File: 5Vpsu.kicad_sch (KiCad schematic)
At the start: 20 parts, among them J8 Conn_01x04_Pin, J9 Conn_01x04_Pin, U7 TPS54360BDDAR

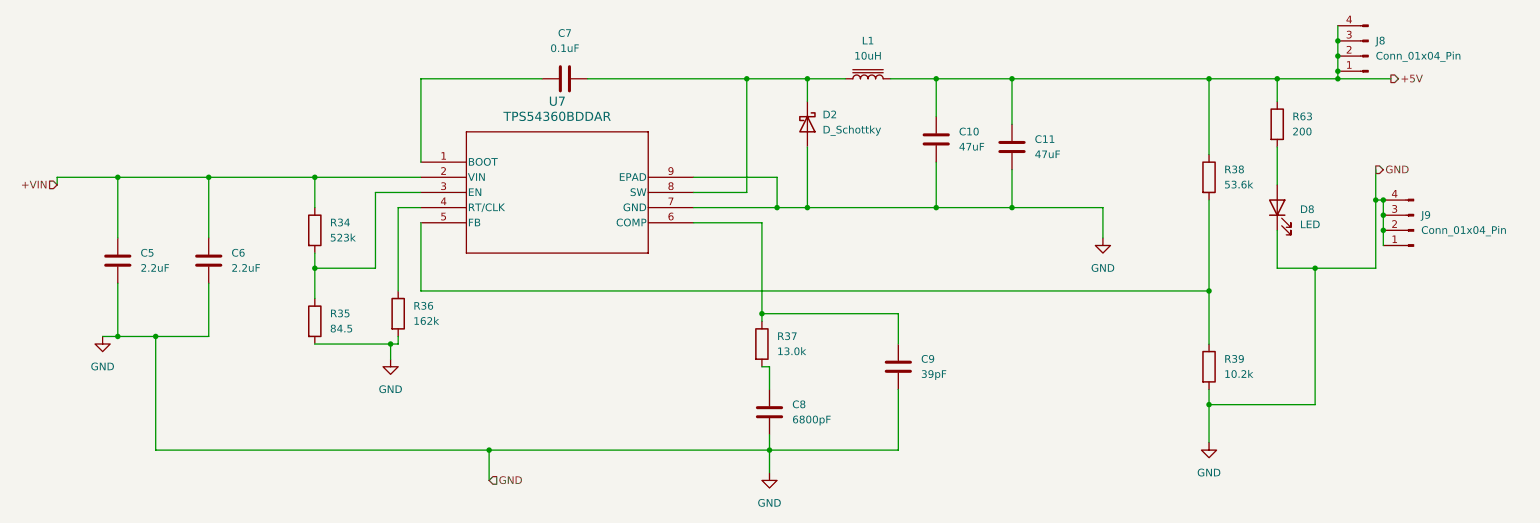
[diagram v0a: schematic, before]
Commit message: switch to cheaper components.
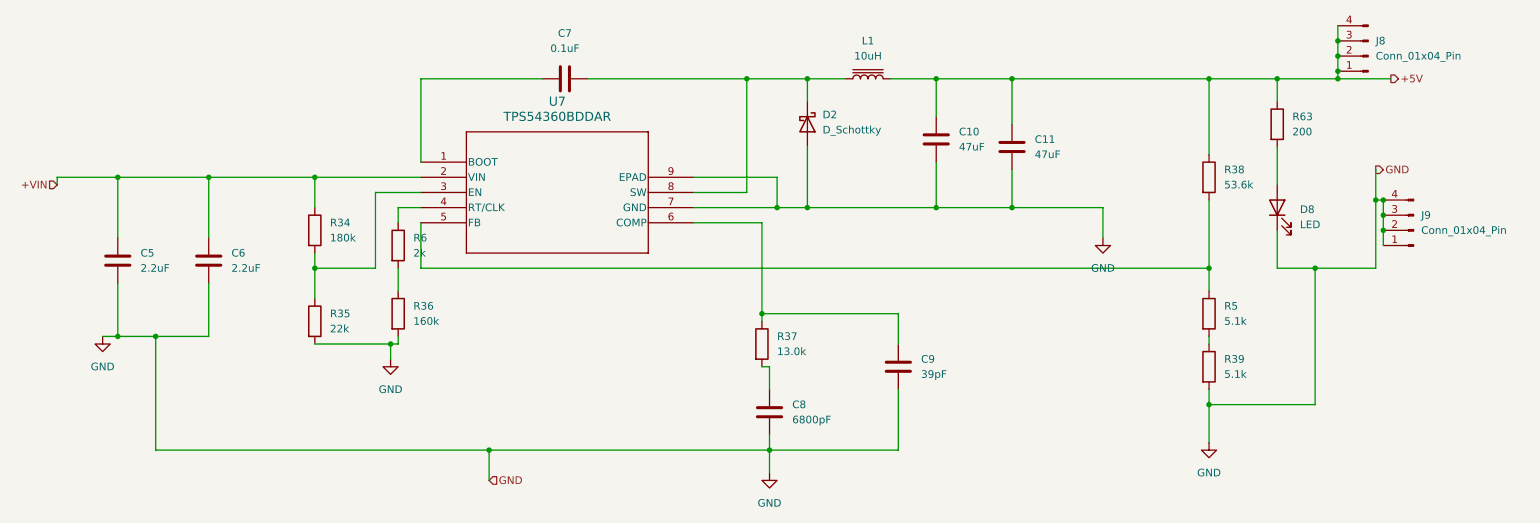
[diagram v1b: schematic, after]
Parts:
- added R5: 5.1k, Resistor_SMD:R_0603_1608Metric, symbol Device:R
- added R6: 2k, Resistor_SMD:R_0603_1608Metric, symbol Device:R
- R34: value 523k -> 180k
- R35: value 84.5 -> 22k
- R36: value 162k -> 160k; LCSC (none) -> C22813
- R39: value 10.2k -> 5.1k
- R63: LCSC (none) -> C8218
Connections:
- net at R38.2, U7.5 (FB): now also R5.1; no longer R39.1
- net at R36.1: now also R6.2; no longer U7.4 (RT/CLK)
- new net: R39.1, R5.2
- new net: R6.1, U7.4 (RT/CLK)
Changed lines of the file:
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@@
+	)
+	(junction
+		(at 223.52 74.93)
+		(diameter 0)
+		(color 0 0 0 0)
 	)
 	(junction
@@
 	)
 	(junction
-		(at 223.52 78.74)
-		(diameter 0)
-		(color 0 0 0 0)
-	)
-	(junction
 		(at 55.88 59.69)
 		(diameter 0)
@@
 	(wire
 		(pts
-			(xy 91.44 78.74) (xy 223.52 78.74)
+			(xy 91.44 74.93) (xy 223.52 74.93)
 		)
 		(stroke
@@
 	(wire
 		(pts
-			(xy 223.52 63.5) (xy 223.52 78.74)
-		)
-		(stroke
-			(width 0)
-			(type default)
-		)
-	)
-	(wire
-		(pts
-			(xy 87.63 64.77) (xy 87.63 78.74)
+			(xy 223.52 63.5) (xy 223.52 74.93)
+		)
+		(stroke
+			(width 0)
+			(type default)
+		)
+	)
+	(wire
+		(pts
+			(xy 87.63 64.77) (xy 87.63 67.31)
 		)
 		(stroke
@@
 	(wire
 		(pts
-			(xy 91.44 67.31) (xy 91.44 78.74)
+			(xy 91.44 67.31) (xy 91.44 74.93)
 		)
 		(stroke
@@
 	(wire
 		(pts
+			(xy 223.52 74.93) (xy 223.52 78.74)
+		)
+		(stroke
+			(width 0)
+			(type default)
+		)
+	)
+	(wire
+		(pts
 			(xy 46.99 105.41) (xy 46.99 86.36)
 		)
@@
 	(wire
 		(pts
+			(xy 223.52 86.36) (xy 223.52 87.63)
+		)
+		(stroke
+			(width 0)
+			(type default)
+		)
+	)
+	(wire
+		(pts
 			(xy 148.59 91.44) (xy 149.86 91.44)
 		)
@@
 	(wire
 		(pts
-			(xy 223.52 78.74) (xy 223.52 87.63)
-		)
-		(stroke
-			(width 0)
-			(type default)
-		)
-	)
-	(wire
-		(pts
 			(xy 149.86 91.44) (xy 149.86 95.25)
 		)
@@
 		(pts
 			(xy 251.46 74.93) (xy 241.3 74.93)
+		)
+		(stroke
+			(width 0)
+			(type default)
+		)
+	)
+	(wire
+		(pts
+			(xy 87.63 74.93) (xy 87.63 78.74)
 		)
 		(stroke
@@
 			)
 		)
-		(property "Value" "523k"
+		(property "Value" "180k"
 			(at 76.2 69.8499 0)
 			(effects
@@
 			)
 		)
-		(property "Value" "84.5"
+		(property "Value" "22k"
 			(at 76.2 85.0899 0)
 			(effects
@@
 			)
 		)
-		(property "Value" "10.2k"
+		(property "Value" "5.1k"
 			(at 226.06 92.7099 0)
 			(effects
@@
 			)
 		)
-		(property "Value" "162k"
+		(property "Value" "160k"
 			(at 90.17 83.8199 0)
 			(effects
@@
 		)
 		(property "Description" "Resistor"
+			(at 87.63 82.55 0)
+			(effects
+				(font
+					(size 1.27 1.27)
+				)
+				(hide yes)
+			)
+		)
+		(property "LCSC" "C22813"
 			(at 87.63 82.55 0)
 			(effects
@@
 			)
 		)
-		(property "LCSC" ""
+		(property "LCSC" "C8218"
 			(at 234.95 50.8 0)
 			(effects
@@
 					(unit 1)
 				)
+			)
+		)
+	)
+	(symbol
+		(lib_id "Device:R")
+		(at 87.63 71.12 0)
+		(unit 1)
+		(exclude_from_sim no)
+		(in_bom yes)
+		(on_board yes)
+		(dnp no)
+		(fields_autoplaced yes)
+		(property "Reference" "R6"
+			(at 90.17 69.8499 0)
+			(effects
+				(font
+					(size 1.27 1.27)
+				)
+				(justify left)
+			)
+		)
+		(property "Value" "2k"
+			(at 90.17 72.3899 0)
+			(effects
+				(font
+					(size 1.27 1.27)
+				)
+				(justify left)
+			)
+		)
+		(property "Footprint" "Resistor_SMD:R_0603_1608Metric"
+			(at 85.852 71.12 90)
+			(effects
+				(font
+					(size 1.27 1.27)
+				)
+				(hide yes)
+			)
+		)
+		(property "Datasheet" "~"
+			(at 87.63 71.12 0)
+			(effects
+				(font
+					(size 1.27 1.27)
+				)
+				(hide yes)
+			)
+		)
+		(property "Description" "Resistor"
+			(at 87.63 71.12 0)
+			(effects
+				(font
+					(size 1.27 1.27)
+				)
+				(hide yes)
+			)
+		)
+		(property "LCSC" "C22975"
+			(at 87.63 71.12 0)
+			(effects
+				(font
+					(size 1.27 1.27)
+				)
+				(hide yes)
+			)
+		)
+		(pin "1"
+		)
+		(pin "2"
+		)
+		(instances
+			(project "dmx"
+				(path "/860489ce-8e24-49a4-b6b1-5a2692123cd9/d5073347-b54d-4371-a8da-3b4e9f26b70c"
+					(reference "R6")
+					(unit 1)
+				)
+			)
+		)
+	)
+	(symbol
+		(lib_id "Device:R")
+		(at 223.52 82.55 0)
+		(unit 1)
+		(exclude_from_sim no)
+		(in_bom yes)
+		(on_board yes)
+		(dnp no)
+		(fields_autoplaced yes)
+		(property "Reference" "R5"
+			(at 226.06 81.2799 0)
+			(effects
+				(font
+					(size 1.27 1.27)
+				)
+				(justify left)
+			)
+		)
+		(property "Value" "5.1k"
+			(at 226.06 83.8199 0)
+			(effects
+				(font
+					(size 1.27 1.27)
+				)
+				(justify left)
+			)
+		)
+		(property "Footprint" "Resistor_SMD:R_0603_1608Metric"
+			(at 221.742 82.55 90)
+			(effects
+				(font
+					(size 1.27 1.27)
+				)
+				(hide yes)
+			)
+		)
+		(property "Datasheet" "~"
+			(at 223.52 82.55 0)
+			(effects
+				(font
+					(size 1.27 1.27)
+				)
+				(hide yes)
+			)
+		)
+		(property "Description" "Resistor"
+			(at 223.52 82.55 0)
+			(effects
+				(font
+					(size 1.27 1.27)
+				)
+				(hide yes)
+			)
+		)
+		(pin "1"
+		)
+		(pin "2"
+		)
+		(instances
+			(project "dmx"
+				(path "/860489ce-8e24-49a4-b6b1-5a2692123cd9/d5073347-b54d-4371-a8da-3b4e9f26b70c"
+					(reference "R5")
+					(unit 1)
+				)

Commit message: replace extended components with basic components.
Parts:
- removed R5: 5.1k, Resistor_SMD:R_0603_1608Metric, symbol Device:R
- added C12: 10uF, Capacitor_SMD:C_0805_2012Metric, symbol Device:C
- added C13: 22pF, Capacitor_SMD:C_0603_1608Metric, symbol Device:C
- added C15: C_Polarized, Capacitor_THT:CP_Radial_D5.0mm_P2.50mm, symbol Device:C_Polarized
- added C2, C3: 22uF, Capacitor_SMD:C_0805_2012Metric, symbol Device:C
- C10, C11: value 47uF -> 22uF; footprint Capacitor_SMD:C_0603_1608Metric -> Capacitor_SMD:C_0805_2012Metric; LCSC (none) -> C45783
- C5, C6: footprint Capacitor_SMD:C_0603_1608Metric -> Capacitor_SMD:C_0805_2012Metric; LCSC (none) -> C377773
- C8: value 6800pF -> 6800pF/6.8nF; LCSC (none) -> C1631
- C9: value 39pF -> 18pF; LCSC (none) -> C1653
- R37: value 13.0k -> 13k
- R38: value 53.6k -> 68k; LCSC (none) -> C23231
- R39: value 5.1k -> 13k; LCSC (none) -> C22797
- R63: value 200 -> 150; footprint Resistor_SMD:R_0805_2012Metric -> Resistor_SMD:R_0603_1608Metric
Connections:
- net +5V: now also C12.2, C2.2, C3.2
- net +VIN: now also C15.1
- net GND: now also C12.1, C13.1, C15.2, C2.1, C3.1
- net at C9.2, R37.1, U7.6 (COMP): now also C13.2
- net at R38.2, U7.5 (FB): now also R39.1

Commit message: change some last parts.
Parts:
- C5, C6: footprint Capacitor_SMD:C_0805_2012Metric -> Capacitor_SMD:C_1206_3216Metric_Pad1.33x1.80mm_HandSolder; LCSC C377773 -> C1021612
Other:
- moved on the sheet: C5
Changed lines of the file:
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@@
+	)
+	(junction
+		(at 45.72 59.69)
+		(diameter 0)
+		(color 0 0 0 0)
 	)
 	(junction
@@
 	)
 	(junction
+		(at 45.72 86.36)
+		(diameter 0)
+		(color 0 0 0 0)
+	)
+	(junction
 		(at 200.66 64.77)
 		(diameter 0)
@@
 	)
 	(junction
-		(at 40.64 86.36)
-		(diameter 0)
-		(color 0 0 0 0)
-	)
-	(junction
 		(at 252.73 66.04)
 		(diameter 0)
@@
 	)
 	(junction
-		(at 40.64 59.69)
-		(diameter 0)
-		(color 0 0 0 0)
-	)
-	(junction
 		(at 73.66 59.69)
 		(diameter 0)
@@
 	(wire
 		(pts
-			(xy 40.64 86.36) (xy 38.1 86.36)
+			(xy 38.1 86.36) (xy 45.72 86.36)
 		)
 		(stroke
@@
 	(wire
 		(pts
-			(xy 40.64 59.69) (xy 40.64 69.85)
+			(xy 45.72 59.69) (xy 45.72 74.93)
 		)
 		(stroke
@@
 	(wire
 		(pts
-			(xy 46.99 86.36) (xy 40.64 86.36)
+			(xy 46.99 86.36) (xy 45.72 86.36)
 		)
 		(stroke
@@
 	(wire
 		(pts
-			(xy 55.88 59.69) (xy 40.64 59.69)
+			(xy 55.88 59.69) (xy 45.72 59.69)
 		)
 		(stroke
@@
 	(wire
 		(pts
-			(xy 40.64 77.47) (xy 40.64 86.36)
+			(xy 45.72 82.55) (xy 45.72 86.36)
 		)
 		(stroke
@@
 	(wire
 		(pts
-			(xy 40.64 59.69) (xy 34.29 59.69)
+			(xy 34.29 59.69) (xy 45.72 59.69)
 		)
 		(stroke
@@
 			)
 		)
-		(property "Footprint" "Capacitor_SMD:C_0805_2012Metric"
+		(property "Footprint" "Capacitor_SMD:C_1206_3216Metric_Pad1.33x1.80mm_HandSolder"
 			(at 56.8452 77.47 0)
 			(effects
@@
 			)
 		)
-		(property "LCSC" "C377773"
+		(property "LCSC" "C1021612"
 			(at 55.88 73.66 0)
 			(effects
@@
 	(symbol
 		(lib_id "Device:C")
-		(at 40.64 73.66 0)
+		(at 45.72 78.74 0)
 		(unit 1)
 		(exclude_from_sim no)
@@
 		(fields_autoplaced yes)
 		(property "Reference" "C5"
-			(at 44.45 72.3899 0)
+			(at 49.53 77.4699 0)
 			(effects
 				(font
@@
 		)
 		(property "Value" "2.2uF"
-			(at 44.45 74.9299 0)
+			(at 49.53 80.0099 0)
 			(effects
 				(font
@@
 			)
 		)
-		(property "Footprint" "Capacitor_SMD:C_0805_2012Metric"
-			(at 41.6052 77.47 0)
+		(property "Footprint" "Capacitor_SMD:C_1206_3216Metric_Pad1.33x1.80mm_HandSolder"
+			(at 46.6852 82.55 0)
 			(effects
 				(font
@@
 		)
 		(property "Datasheet" "~"
-			(at 40.64 73.66 0)
+			(at 45.72 78.74 0)
 			(effects
 				(font
@@
 		)
 		(property "Description" "Unpolarized capacitor"
-			(at 40.64 73.66 0)
-			(effects
-				(font
-					(size 1.27 1.27)
-				)
-				(hide yes)
-			)
-		)
-		(property "LCSC" "C377773"
-			(at 40.64 73.66 0)
-			(effects
-				(font
+			(at 45.72 78.74 0)
+			(effects
+				(font
+					(size 1.27 1.27)
+				)
+				(hide yes)
+			)
+		)
+		(property "LCSC" "C1021612"
+			(at 45.72 78.74 0)
+			(effects
+				(font
